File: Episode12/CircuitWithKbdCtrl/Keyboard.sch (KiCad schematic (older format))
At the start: 13 parts, among them J501 Conn_01x20, U501 87C51/89C51, U502 IDT7201, U503 74LS138, U504 74HCT541, Y501 11.0592 MHz

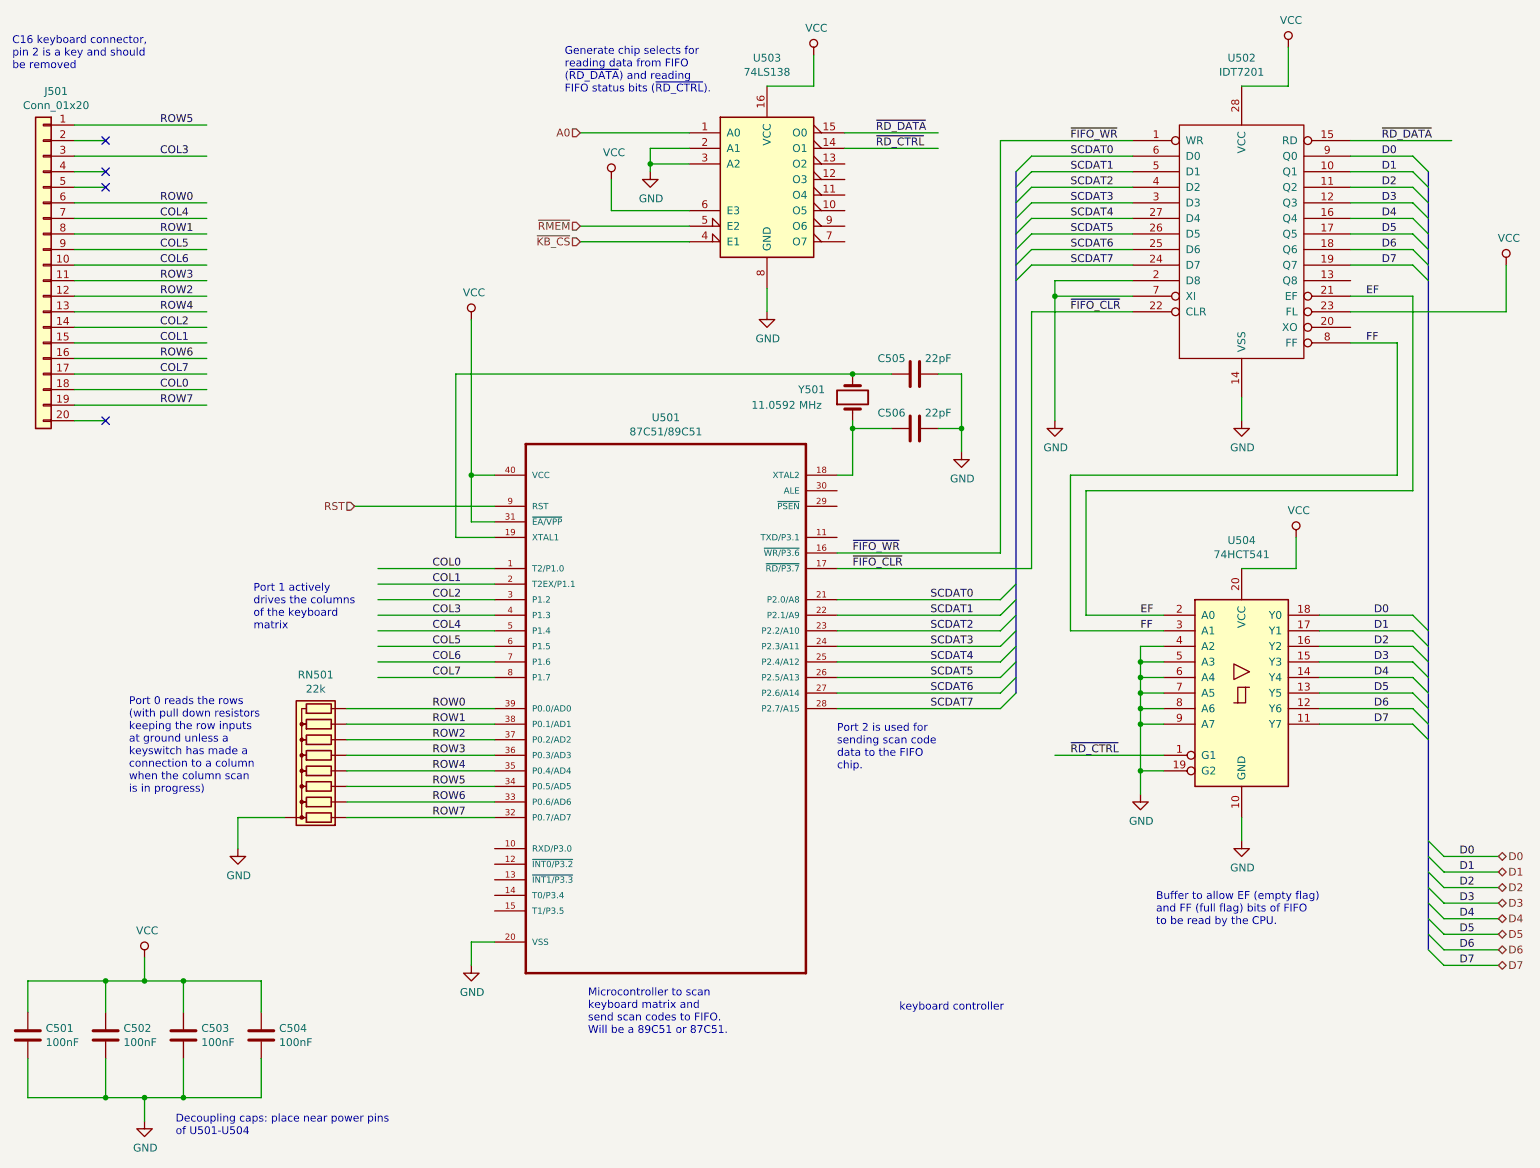
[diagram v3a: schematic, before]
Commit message: use pull ups rather than pull downs on row inputs
Port 1 seems to have trouble driving a high output
when there is a pull down resistor.  It's possible
that driving to ground against a pull up resistor
will work better (would make sense, because the 8051
family normally drives LEDs by connecting the
cathode of the LED to the output and driving the
output low to light the LED.)
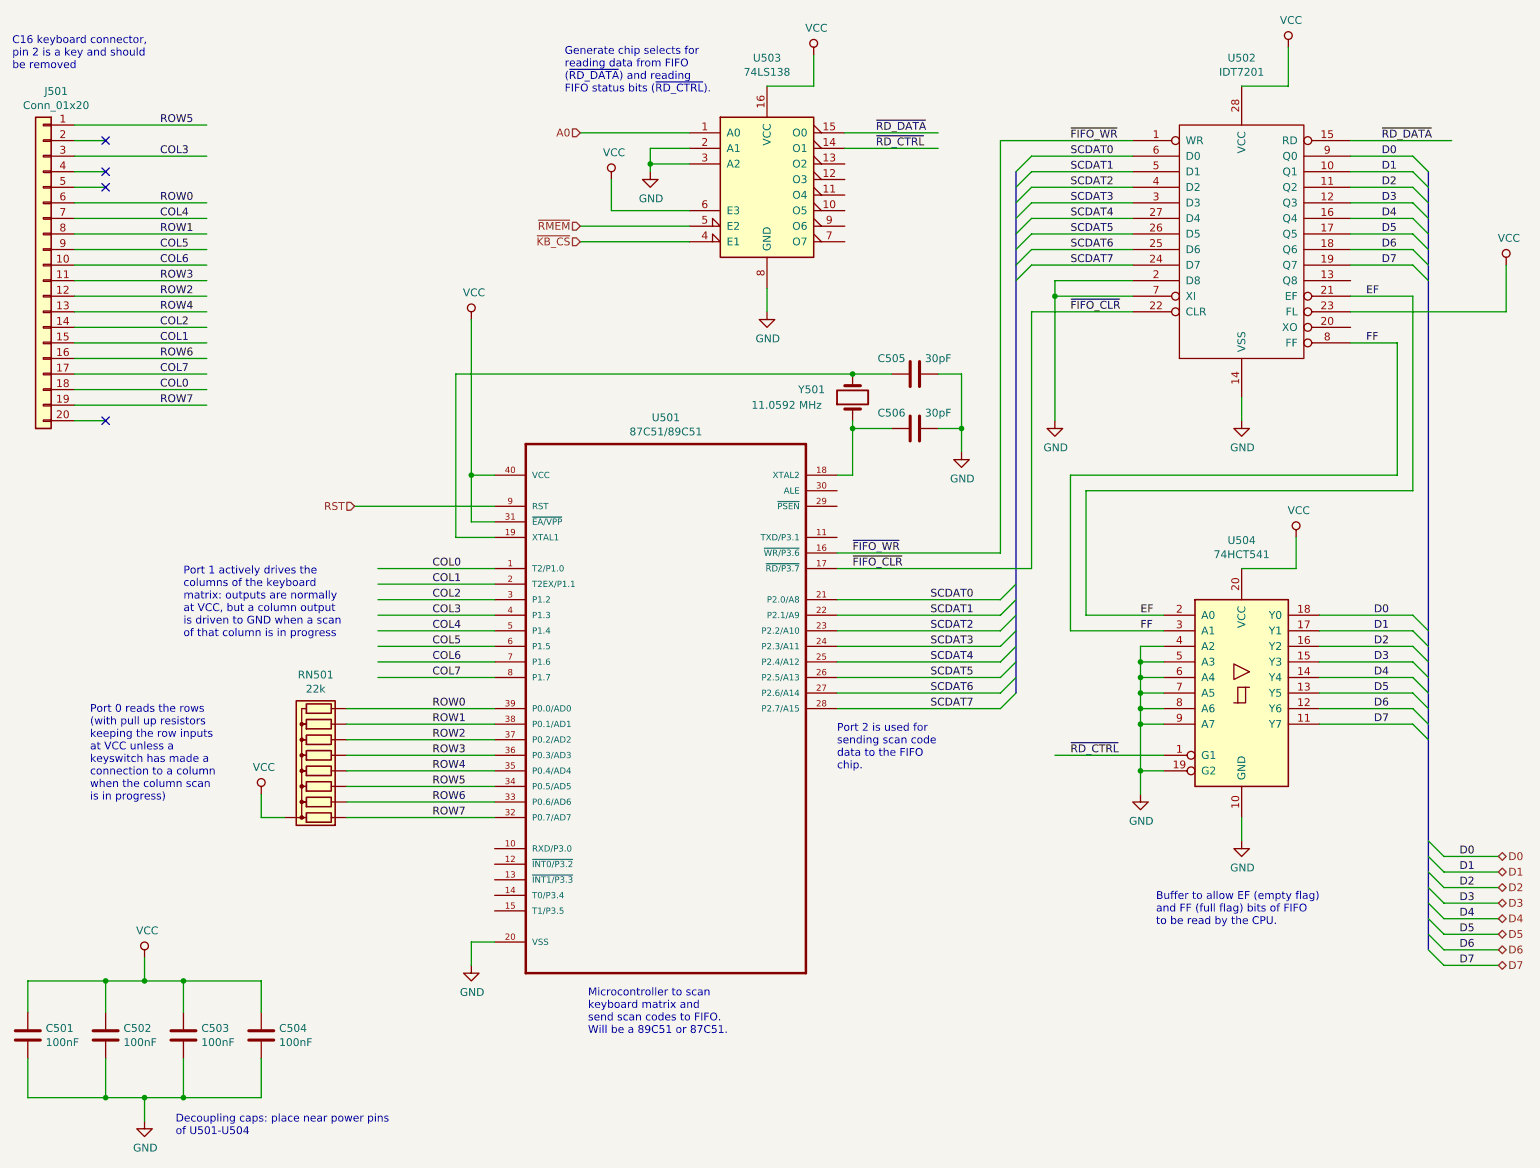
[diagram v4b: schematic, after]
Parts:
- C505, C506: value 22pF -> 30pF
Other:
- note added: "Port 0 reads the rows\n(with pull up resistors\nkeeping the row inputs\nat VCC unless a\nkeyswitch has made a\nconnection to a column\nwhen the column scan\nis in progress)"
- note added: "Port 1 actively drives the\ncolumns of the keyboard\nmatrix: outputs are normally\nat VCC, but a column output\nis driven to GND when a scan\nof that column is in progress"
- note removed: "Port 0 reads the rows\n(with pull down resistors\nkeeping the row inputs\nat ground unless a\nkeyswitch has made a\nconnection to a column\nwhen the column scan\nis in progress)"
- note removed: "Port 1 actively\ndrives the columns\nof the keyboard\nmatrix"
- note removed: "keyboard controller"
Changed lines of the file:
@@
 encoding utf-8
 Sheet 6 6
-Title ""
+Title "keyboard controller"
 Date ""
 Rev ""
-Comp ""
+Comp "daveho hacks"
 Comment1 ""
 Comment2 ""
@@
 $EndComp
 Wire Wire Line
-	2450 5700 2150 5700
+	2450 5700 2300 5700
 Wire Wire Line
 	5050 1400 4800 1400
@@
 Entry Wire Line
 	9800 6550 9900 6650
-Text Notes 6400 6950 0    50   ~ 0
-keyboard controller
 Wire Wire Line
 	9300 2350 9700 2350
@@
 $EndComp
 Wire Wire Line
-	2150 5700 2150 5900
-$Comp
-L power:GND #PWR?
-U 1 1 5EDCA2EA
-P 2150 5900
-F 0 "#PWR?" H 2150 5650 50  0001 C CNN
-F 1 "GND" H 2155 5727 50  0000 C CNN
-F 2 "" H 2150 5900 50  0001 C CNN
-F 3 "" H 2150 5900 50  0001 C CNN
-	1    2150 5900
-	1    0    0    -1
-$EndComp
-Wire Wire Line
 	2850 5100 3800 5100
 Wire Wire Line
@@
 Wire Wire Line
 	2850 5500 3800 5500
-Text Notes 2250 4500 0    50   ~ 0
-Port 1 actively\ndrives the columns\nof the keyboard\nmatrix
-Text Notes 1450 5550 0    50   ~ 0
-Port 0 reads the rows\n(with pull down resistors\nkeeping the row inputs\nat ground unless a\nkeyswitch has made a\nconnection to a column\nwhen the column scan\nis in progress)
+Text Notes 1800 4550 0    50   ~ 0
+Port 1 actively drives the\ncolumns of the keyboard\nmatrix: outputs are normally\nat VCC, but a column output\nis driven to GND when a scan\nof that column is in progress
+Text Notes 1200 5600 0    50   ~ 0
+Port 0 reads the rows\n(with pull up resistors\nkeeping the row inputs\nat VCC unless a\nkeyswitch has made a\nconnection to a column\nwhen the column scan\nis in progress)
 Text Label 6600 4300 0    50   ~ 0
 SCDAT0
@@
 P 6500 2850
 F 0 "C505" V 6400 2700 50  0000 C CNN
-F 1 "22pF" V 6400 3000 50  0000 C CNN
+F 1 "30pF" V 6400 3000 50  0000 C CNN
 F 2 "" H 6538 2700 50  0001 C CNN
 F 3 "" H 6500 2850 50  0001 C CNN
@@
 P 6500 3200
 F 0 "C506" V 6400 3050 50  0000 C CNN
-F 1 "22pF" V 6400 3350 50  0000 C CNN
+F 1 "30pF" V 6400 3350 50  0000 C CNN
 F 2 "" H 6538 3050 50  0001 C CNN
 F 3 "" H 6500 3200 50  0001 C CNN
@@
 Text Label 1650 2050 0    50   ~ 0
 COL5
+Wire Wire Line
+	2300 5700 2300 5550
+$Comp
+L power:VCC #PWR?
+U 1 1 5ED20CD9
+P 2300 5550
+F 0 "#PWR?" H 2300 5400 50  0001 C CNN
+F 1 "VCC" H 2317 5723 50  0000 C CNN
+F 2 "" H 2300 5550 50  0001 C CNN
+F 3 "" H 2300 5550 50  0001 C CNN
+	1    2300 5550
+	1    0    0    -1
+$EndComp
 Wire Bus Line
 	7150 1550 7150 4900

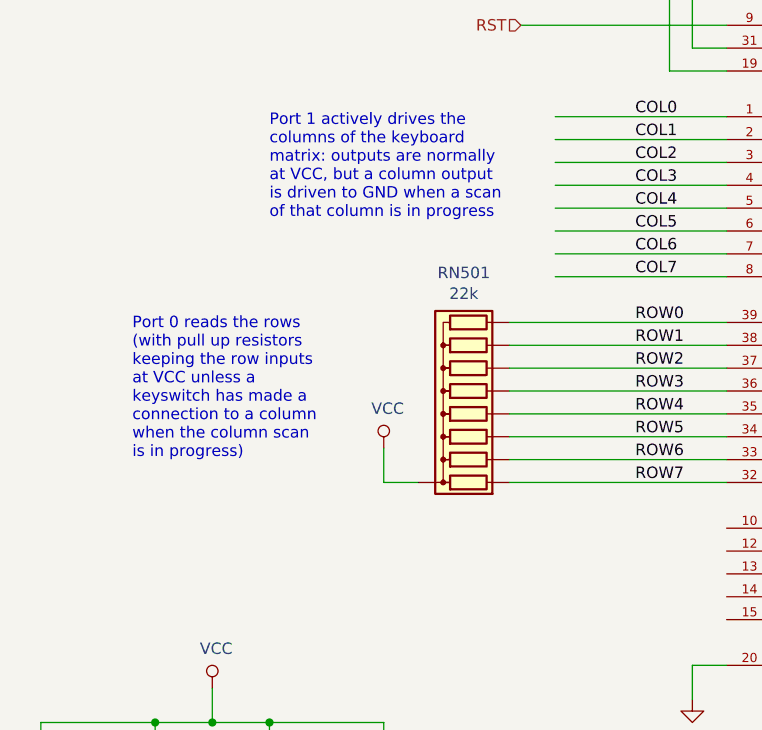
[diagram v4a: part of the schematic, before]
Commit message: go back to using pull-down resistors on row inputs
P1's output can't seem to drive an output to ground
strongly enough to overcome even extremely weak pull
up resistors.
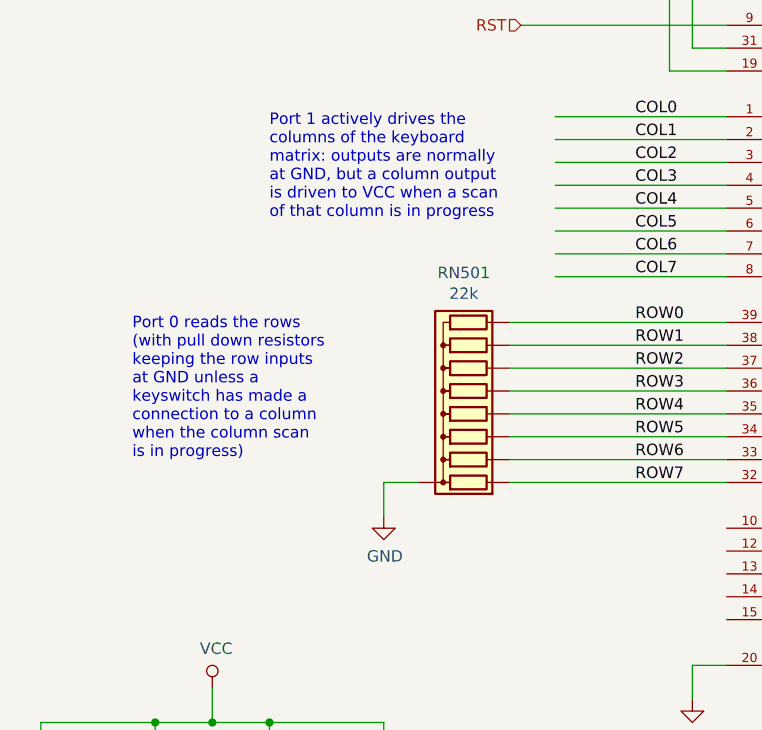
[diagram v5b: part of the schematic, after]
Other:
- note added: "Port 0 reads the rows\n(with pull down resistors\nkeeping the row inputs\nat GND unless a\nkeyswitch has made a\nconnection to a column\nwhen the column scan\nis in progress)"
- note added: "Port 1 actively drives the\ncolumns of the keyboard\nmatrix: outputs are normally\nat GND, but a column output\nis driven to VCC when a scan\nof that column is in progress"
- note removed: "Port 0 reads the rows\n(with pull up resistors\nkeeping the row inputs\nat VCC unless a\nkeyswitch has made a\nconnection to a column\nwhen the column scan\nis in progress)"
- note removed: "Port 1 actively drives the\ncolumns of the keyboard\nmatrix: outputs are normally\nat VCC, but a column output\nis driven to GND when a scan\nof that column is in progress"
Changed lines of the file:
@@
 	2850 5500 3800 5500
 Text Notes 1800 4550 0    50   ~ 0
-Port 1 actively drives the\ncolumns of the keyboard\nmatrix: outputs are normally\nat VCC, but a column output\nis driven to GND when a scan\nof that column is in progress
+Port 1 actively drives the\ncolumns of the keyboard\nmatrix: outputs are normally\nat GND, but a column output\nis driven to VCC when a scan\nof that column is in progress
 Text Notes 1200 5600 0    50   ~ 0
-Port 0 reads the rows\n(with pull up resistors\nkeeping the row inputs\nat VCC unless a\nkeyswitch has made a\nconnection to a column\nwhen the column scan\nis in progress)
+Port 0 reads the rows\n(with pull down resistors\nkeeping the row inputs\nat GND unless a\nkeyswitch has made a\nconnection to a column\nwhen the column scan\nis in progress)
 Text Label 6600 4300 0    50   ~ 0
 SCDAT0
@@
 COL5
 Wire Wire Line
-	2300 5700 2300 5550
-$Comp
-L power:VCC #PWR?
-U 1 1 5ED20CD9
-P 2300 5550
-F 0 "#PWR?" H 2300 5400 50  0001 C CNN
-F 1 "VCC" H 2317 5723 50  0000 C CNN
-F 2 "" H 2300 5550 50  0001 C CNN
-F 3 "" H 2300 5550 50  0001 C CNN
-	1    2300 5550
-	1    0    0    -1
-$EndComp
+	2300 5700 2300 5850
 Wire Bus Line
 	7150 1550 7150 4900
 Wire Bus Line
 	9800 1550 9800 6550
+$Comp
+L power:GND #PWR?
+U 1 1 5ED1C2BF
+P 2300 5850
+F 0 "#PWR?" H 2300 5600 50  0001 C CNN
+F 1 "GND" H 2305 5677 50  0000 C CNN
+F 2 "" H 2300 5850 50  0001 C CNN
+F 3 "" H 2300 5850 50  0001 C CNN
+	1    2300 5850
+	1    0    0    -1
+$EndComp
 $EndSCHEMATC

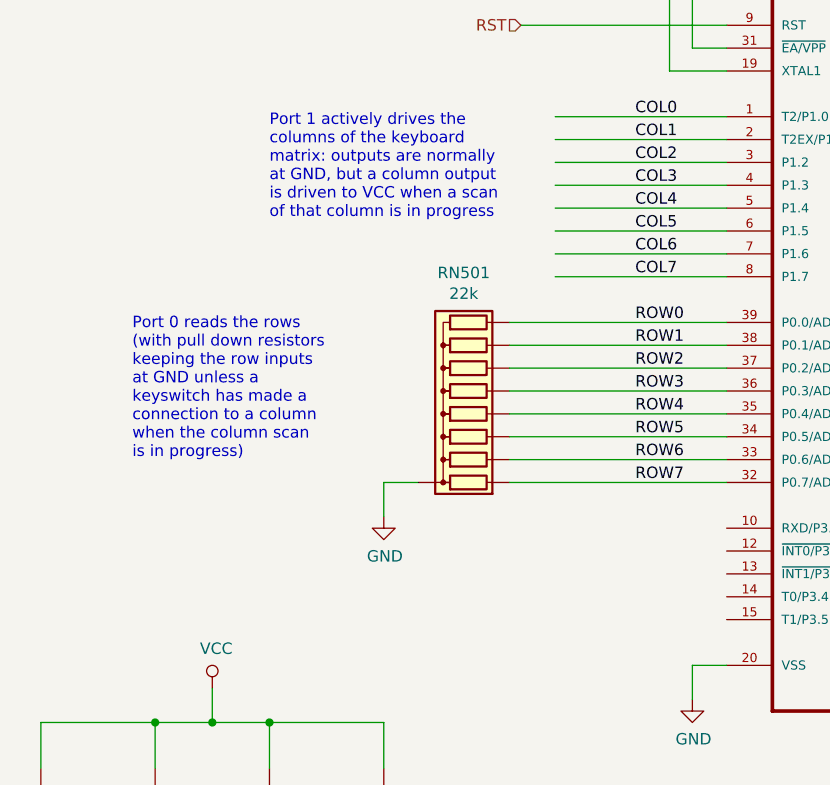
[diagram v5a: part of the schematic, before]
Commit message: use pull-down resistors on row inputs
The reason it wasn't working before was actually
a firmware bug: multiple columns were being driven
to GND simultaneously.  With that bug fixed,
it now seems to be working perfectly.
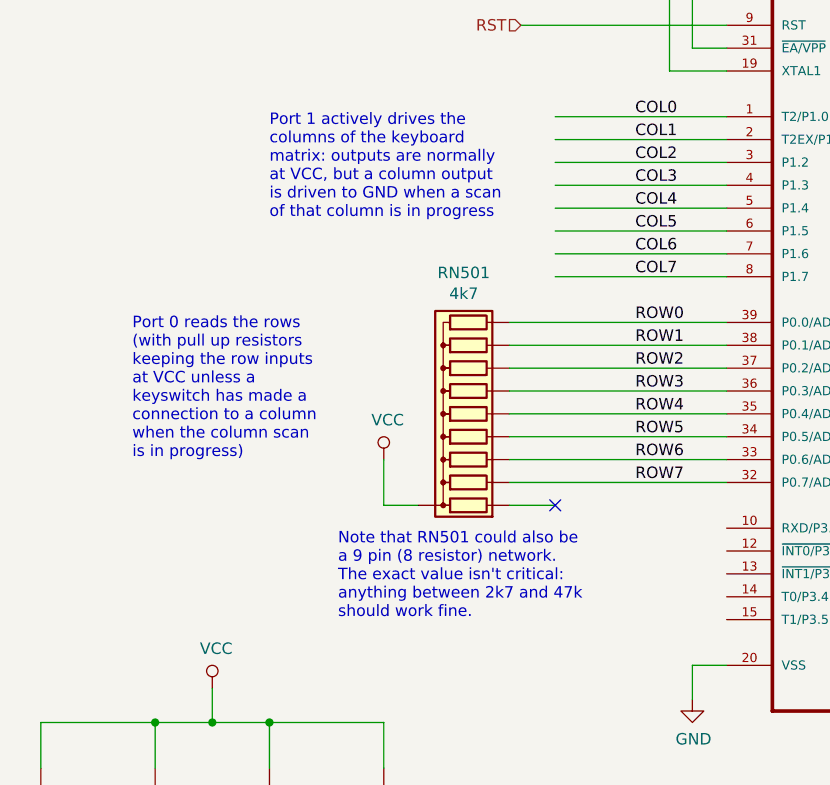
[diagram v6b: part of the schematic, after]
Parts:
- removed RN501: 22k, Resistors_THT:R_Array_SIP9, symbol device:R_Network08
- added RN501: 4k7, Resistors_THT:R_Array_SIP10, symbol device:R_Network09
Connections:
- wire segments 173 -> 174
- no-connect marks 4 -> 5
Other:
- note added: "Note that RN501 could also be\na 9 pin (8 resistor) network.\nThe exact value isn't critical:\nanything between 2k7 and 47k\nshould work fine."
- note added: "Port 0 reads the rows\n(with pull up resistors\nkeeping the row inputs\nat VCC unless a\nkeyswitch has made a\nconnection to a column\nwhen the column scan\nis in progress)"
- note added: "Port 1 actively drives the\ncolumns of the keyboard\nmatrix: outputs are normally\nat VCC, but a column output\nis driven to GND when a scan\nof that column is in progress"
- note removed: "Port 0 reads the rows\n(with pull down resistors\nkeeping the row inputs\nat GND unless a\nkeyswitch has made a\nconnection to a column\nwhen the column scan\nis in progress)"
- note removed: "Port 1 actively drives the\ncolumns of the keyboard\nmatrix: outputs are normally\nat GND, but a column output\nis driven to VCC when a scan\nof that column is in progress"
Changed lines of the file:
@@
 Text Label 3400 5700 0    50   ~ 0
 ROW7
-$Comp
-L device:R_Network08 RN501
-U 1 1 5E35B9F3
-P 2650 5300
-F 0 "RN501" V 3167 5300 50  0000 C CNN
-F 1 "22k" V 3076 5300 50  0000 C CNN
-F 2 "Resistors_THT:R_Array_SIP9" V 3125 5300 50  0001 C CNN
-F 3 "" H 2650 5300 50  0001 C CNN
-	1    2650 5300
-	0    -1   -1   0
-$EndComp
-Wire Wire Line
-	2450 5700 2300 5700
+Wire Wire Line
+	2450 5800 2300 5800
 Wire Wire Line
 	5050 1400 4800 1400
@@
 	2850 5500 3800 5500
 Text Notes 1800 4550 0    50   ~ 0
-Port 1 actively drives the\ncolumns of the keyboard\nmatrix: outputs are normally\nat GND, but a column output\nis driven to VCC when a scan\nof that column is in progress
+Port 1 actively drives the\ncolumns of the keyboard\nmatrix: outputs are normally\nat VCC, but a column output\nis driven to GND when a scan\nof that column is in progress
 Text Notes 1200 5600 0    50   ~ 0
-Port 0 reads the rows\n(with pull down resistors\nkeeping the row inputs\nat GND unless a\nkeyswitch has made a\nconnection to a column\nwhen the column scan\nis in progress)
+Port 0 reads the rows\n(with pull up resistors\nkeeping the row inputs\nat VCC unless a\nkeyswitch has made a\nconnection to a column\nwhen the column scan\nis in progress)
 Text Label 6600 4300 0    50   ~ 0
 SCDAT0
@@
 Text Label 1650 2050 0    50   ~ 0
 COL5
-Wire Wire Line
-	2300 5700 2300 5850
+$Comp
+L device:R_Network09 RN501
+U 1 1 5ED1E896
+P 2650 5400
+F 0 "RN501" V 3267 5400 50  0000 C CNN
+F 1 "4k7" V 3176 5400 50  0000 C CNN
+F 2 "Resistors_THT:R_Array_SIP10" V 3225 5400 50  0001 C CNN
+F 3 "" H 2650 5400 50  0001 C CNN
+	1    2650 5400
+	0    -1   -1   0
+$EndComp
+Wire Wire Line
+	2300 5800 2300 5600
+$Comp
+L power:VCC #PWR?
+U 1 1 5ED640C7
+P 2300 5600
+F 0 "#PWR?" H 2300 5450 50  0001 C CNN
+F 1 "VCC" H 2317 5773 50  0000 C CNN
+F 2 "" H 2300 5600 50  0001 C CNN
+F 3 "" H 2300 5600 50  0001 C CNN
+	1    2300 5600
+	1    0    0    -1
+$EndComp
+Wire Wire Line
+	2850 5800 3050 5800
+NoConn ~ 3050 5800
 Wire Bus Line
 	7150 1550 7150 4900
 Wire Bus Line
 	9800 1550 9800 6550
-$Comp
-L power:GND #PWR?
-U 1 1 5ED1C2BF
-P 2300 5850
-F 0 "#PWR?" H 2300 5600 50  0001 C CNN
-F 1 "GND" H 2305 5677 50  0000 C CNN
-F 2 "" H 2300 5850 50  0001 C CNN
-F 3 "" H 2300 5850 50  0001 C CNN
-	1    2300 5850
-	1    0    0    -1
-$EndComp
+Text Notes 2100 6300 0    50   ~ 0
+Note that RN501 could also be\na 9 pin (8 resistor) network.\nThe exact value isn't critical:\nanything between 2k7 and 47k\nshould work fine.
 $EndSCHEMATC
